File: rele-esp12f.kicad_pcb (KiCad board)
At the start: 2 copper layers, 66.5 x 44 mm, 31 parts, among them J1 N / L_OUT / L_IN, J3 PROG, K1 SRD-05VDC-SL-C, Q1 SS8050, SW1 TS-1187A, SW2 TS-1187A, U1 AMS1117-3.3, U2 ESP-12F

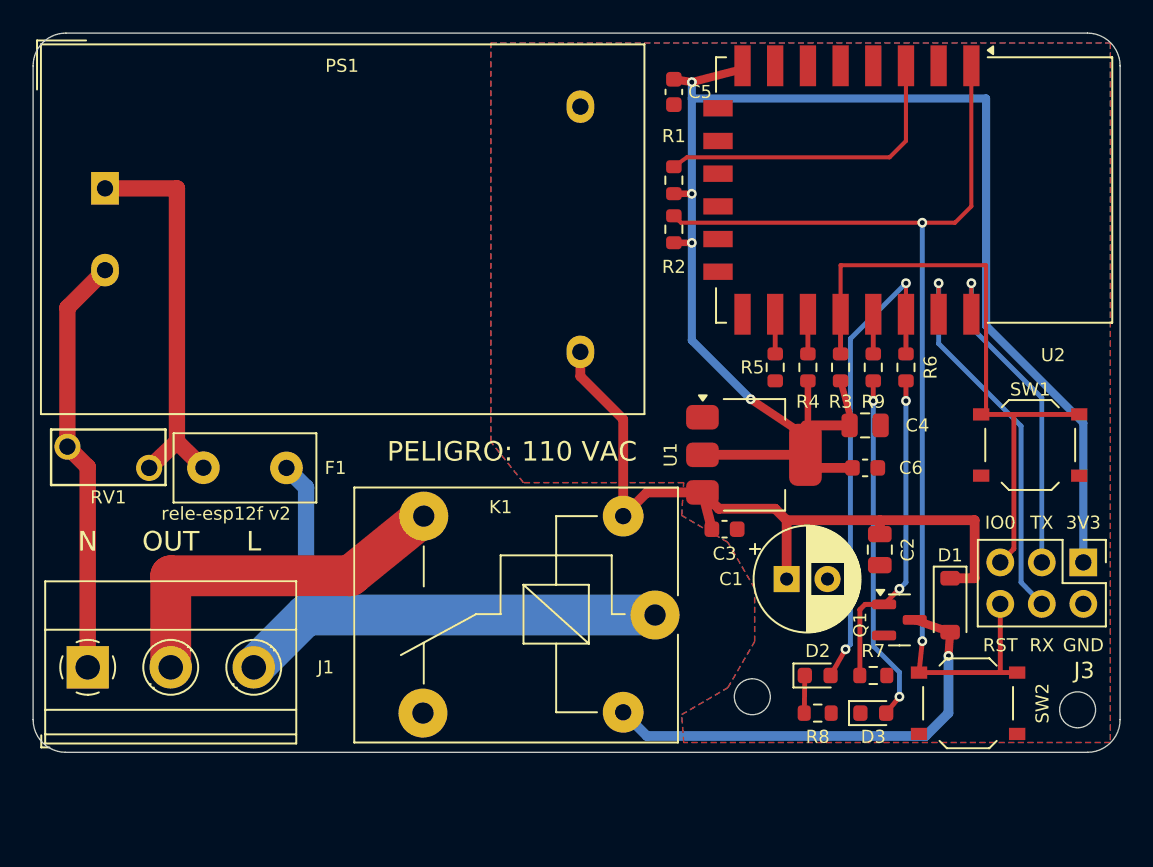
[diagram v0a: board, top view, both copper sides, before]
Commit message: v3 revision: Omron G5RL relay, 10 A load and complete documentation
  Hardware
  - Omron G5RL-1A-E-HR relay (16 A, reinforced insulation) instead of
    the SRD-05VDC; 66.5 x 49 mm board.
  - Power path duplicated on both sides (2 x 2.5 mm) for 10 A.
  - J3 powered at 5 V; RC delay on EN/RST (C7, C8) and 10 uF
    decoupling next to the ESP-12F (C9).
  - Mains copper >= 2.0 mm from the edge; K1 rule removed so the 4 mm
    mains/low-voltage clearance applies across the whole board.
  - Gerbers, drill files, BOM, CPL, renders and schematic regenerated.
  
  Repository
  - Restructured README, CHANGELOG and CERN-OHL-W-2.0 license.
  - PDF datasheet and user guide with its generator script.
  - 3D-printable enclosure (FreeCAD, STEP and STL).
  - Relay STEP model and datasheets of the key components.
  - Removed the v1 generator scripts and the empty manual BOM.
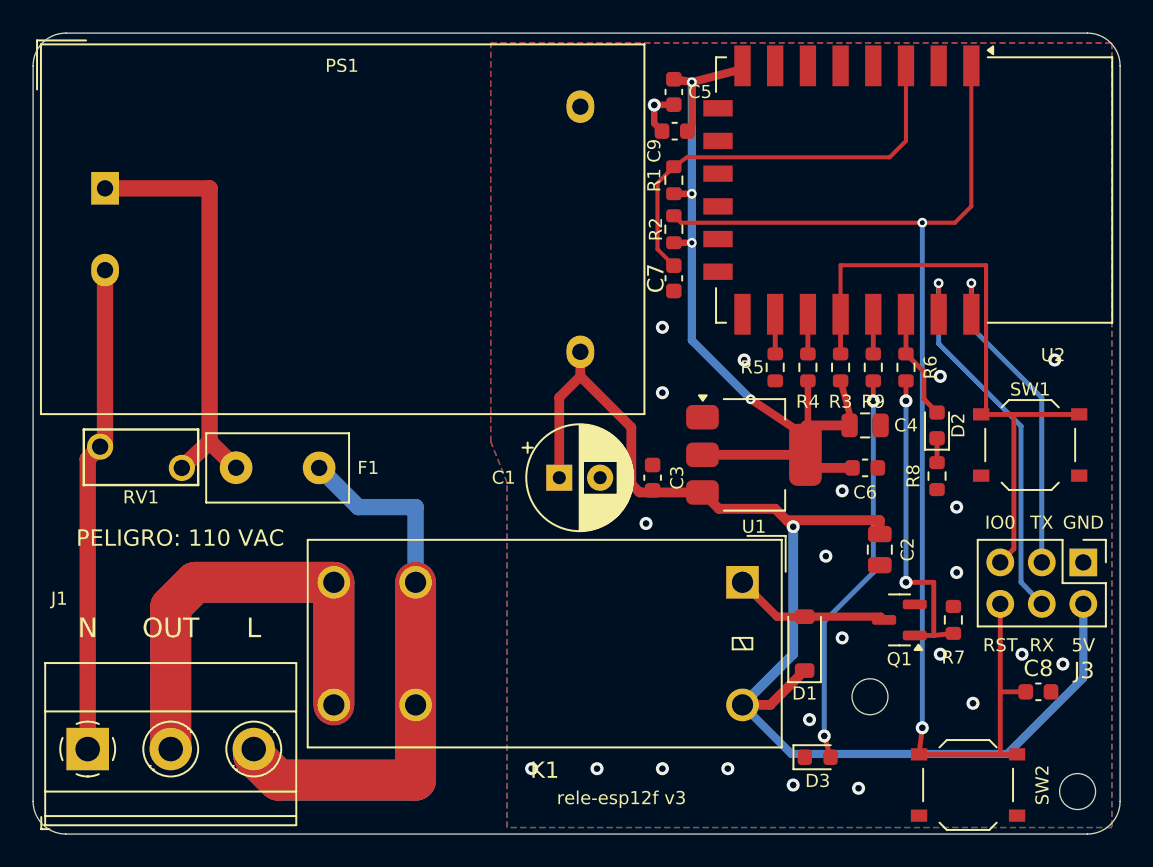
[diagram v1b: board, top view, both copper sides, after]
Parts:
- added C7: 100nF, Capacitor_SMD:C_0603_1608Metric, F.Cu at (139.2, 115.0)
- added C8: 100nF, Capacitor_SMD:C_0603_1608Metric, F.Cu at (161.5, 140.3)
- added C9: 10uF, Capacitor_SMD:C_0603_1608Metric, F.Cu at (139.2, 106.0)
- K1: value SRD-05VDC-SL-C -> G5RL-1A-E-HR DC5; footprint Relay_THT:Relay_SPDT_SANYOU_SRD_Series_Form_C -> Relay_THT:Relay_SPST_Omron_G2RL-1A-E
- moved D2 17.0 mm to (155.3, 124.0), turned to 90 degrees
- moved R8 16.2 mm to (155.3, 127.1), turned to -90 degrees
- moved C1 15.2 mm to (132.2, 127.2)
- moved D1 9.21 mm to (147.2, 137.3), turned to 90 degrees
- moved MH1 7.20 mm to (151.2, 140.6)
- moved R7 5.96 mm to (156.3, 135.9), turned to 90 degrees
- moved K1 5.71 mm to (143.4, 133.6), turned to -90 degrees
- moved C3 5.41 mm to (137.9, 127.2), turned to 90 degrees
- moved J1 5.00 mm to (103.3, 143.8)
- moved MH2 5.00 mm to (163.9, 146.4)
- moved SW2 5.00 mm to (157.2, 146.0)
- moved D3 4.34 mm to (148.0, 144.3)
- moved F1 2.00 mm to (117.5, 126.6)
- moved RV1 2.00 mm to (109.1, 126.6)
- turned Q1 to 180 degrees
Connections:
- J3 pad 1: +3V3 -> GND
- J3 pad 2: GND -> +5V
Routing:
- net +3V3: track 96.1 -> 50.3 mm
- net +5V: track 45.8 -> 79.1 mm, vias 0 -> 1
- net /L_OUT: track 22.4 -> 53.6 mm
- net /L_IN: track 35.4 -> 57.5 mm
- net /RELAY: track 28.9 -> 6.79 mm, vias 2 -> 0
- net /COIL_N: track 28.3 -> 9.61 mm, vias 1 -> 0
- net /RST: track 64.1 -> 75.7 mm
- net /EN: track 18.4 -> 25.3 mm
- net /N: track 25.8 -> 29.7 mm
- net Net-(D3-A): track 21.3 -> 24.3 mm
- net GND: track 0.00 -> 3.00 mm, vias 0 -> 23
- net /L_F: track 24.5 -> 26.5 mm
- net Net-(D2-K): track 2.30 -> 1.48 mm
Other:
- board size 66.5 x 44 mm -> 66.5 x 49 mm
- board text added: "5V"
- board text added: "rele-esp12f v3"
- board text removed: "3V3"
- board text removed: "rele-esp12f v2"

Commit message: Translate the repository to English
- README, CHANGELOG and enclosure README rewritten in English.
- Folders and files renamed: fabrication/, enclosure/, docs/schematic.pdf,
  docs/pcb_top.png, docs/pcb_bottom.png, scripts/generate_datasheet.py.
- Datasheet and user guide regenerated in English (document rev. B).
- Silkscreen "DANGER: 110 VAC", schematic notes, LED values, design rule
  names and the "Assembly" field translated; schematic title block set
  to revision v3. Gerbers, ZIP, renders and schematic PDF regenerated.
- Enclosure script translated and lid label changed to "RELAY"; STL,
  STEP, FreeCAD document and renders regenerated.

DRC: 0 errors, 0 unconnected (29 warnings, unchanged). ERC: 0 errors.
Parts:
- D2: value LED relay (rojo) -> LED relay (red)
- D3: value LED WiFi (azul) -> LED WiFi (blue)
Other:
- board text added: "DANGER: 110 VAC"
- board text removed: "PELIGRO: 110 VAC"
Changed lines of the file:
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@@
 			)
 		)
-		(property "Value" "LED WiFi (azul)"
+		(property "Value" "LED WiFi (blue)"
 			(at 0 1.43 0)
 			(layer "F.Fab")
@@
 			)
 		)
-		(property "Value" "LED relay (rojo)"
+		(property "Value" "LED relay (red)"
 			(at 0.5 2.5 90)
 			(layer "F.Fab")
@@
 		)
 	)
-	(gr_text "PELIGRO: 110 VAC"
+	(gr_text "DANGER: 110 VAC"
 		(at 109 130.9 0)
 		(layer "F.SilkS")
